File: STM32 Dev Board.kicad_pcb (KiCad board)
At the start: 2 copper layers, 41.1 x 50 mm, 33 parts, among them J5 2 Pin JST, J6 USB_B_Micro, Q1 PMOS, U1 FT230XS, U2 STM32F070F6Px, U3 MCP1824S, U4 MCP73113

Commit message: generated drill and gerber files, updeted a few datasheets
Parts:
- removed the D4 at (130.7, 97.0)
- removed the D4 at (127.8, 98.8)
- added C3: 7pF, Capacitor_SMD:C_0805_2012Metric_Pad1.18x1.45mm_HandSolder, F.Cu at (127.9, 85.0)
- added C4: 7pF, Capacitor_SMD:C_0805_2012Metric_Pad1.18x1.45mm_HandSolder, F.Cu at (127.9, 78.4)
- added D4: D_Schottky, Diode_SMD:D_SMF, B.Cu at (151.3, 85.1)
- added R9: 10k, Resistor_SMD:R_1206_3216Metric_Pad1.30x1.75mm_HandSolder, F.Cu at (124.3, 67.6)
- added X1: ~, MyLib:Xtal, F.Cu at (127.1, 82.8)
- J5: footprint Battery:BatteryHolder_MPD_BK-18650-PC2 -> Connector_PinHeader_2.00mm:PinHeader_1x02_P2.00mm_Vertical_SMD_Pin1Right
- SW2: moved to F.Cu
- U1: value FT230XS -> MCP2221AxML; footprint Package_SO:SSOP-16_3.9x4.9mm_P0.635mm -> Package_DFN_QFN:QFN-16-1EP_4x4mm_P0.65mm_EP2.5x2.5mm
- moved J5 86.5 mm to (155.3, 88.1), turned to 180 degrees
- moved J7 50.9 mm to (134.0, 67.7), turned to 0 degrees
- moved J6 46.5 mm to (141.3, 68.8), turned to 180 degrees
- moved SW2 40.8 mm to (125.3, 72.2), turned to -90 degrees
- moved R3 40.5 mm to (141.8, 73.6), turned to 180 degrees
- moved J3 37.1 mm to (130.4, 75.3), turned to 180 degrees
- moved R8 32.0 mm to (151.3, 80.1)
- moved D3 31.1 mm to (156.6, 84.2), turned to -90 degrees
- moved U1 29.9 mm to (140.2, 77.5)
- moved R7 27.7 mm to (153.6, 85.2), turned to -90 degrees
- moved R5 22.0 mm to (156.1, 72.3), turned to 0 degrees
- moved Q1 21.3 mm to (147.6, 81.3)
- moved R4 21.2 mm to (155.6, 75.9), turned to -90 degrees
- moved D1 20.9 mm to (152.8, 69.2), turned to 0 degrees
- moved U4 17.0 mm to (152.8, 72.6), turned to 180 degrees
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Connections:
- J7 pad 3: UART_Rx -> UART_Tx
- J7 pad 4: UART_Tx -> UART_Rx
- R3 pad 1: Net-(U1-~{RESET}) -> VUSB
- R3 pad 2: VUSB -> Net-(U1-~{RST})
- SW2 pad 1: GND -> Net-(R9-Pad1)
- U1 pad 1: UART_Tx -> unconnected-(U1-GP0-Pad1)
- U1 pad 10: Net-(U1-3V3OUT) -> VUSB
- U1 pad 11: Net-(U1-~{RESET}) -> Net-(J6-D-)
- U1 pad 12: VUSB -> Net-(J6-D+)
- U1 pad 16: unconnected-(U1-CBUS3-Pad16) -> VUSB
- U1 pad 3: Net-(U1-3V3OUT) -> Net-(U1-~{RST})
- U1 pad 4: UART_Rx -> UART_Tx
- U1 pad 5: GND -> UART_Rx
- U1 pad 8: Net-(J6-D+) -> unconnected-(U1-SDA-Pad8)
- U1 pad 9: Net-(J6-D-) -> unconnected-(U1-SCL-Pad9)
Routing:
- net Net-(SW2-C): track 0.00 -> 27.4 mm
- net /PSU/BAT+: track 29.9 -> 3.20 mm
- net Net-(U2-PB1): track 27.3 -> 10.4 mm
- net Net-(J6-D+): track 21.8 -> 6.24 mm
- net 3.3V: track 68.4 -> 53.5 mm, vias 4 -> 6
- net Net-(J6-D-): track 22.7 -> 7.69 mm
- net VUSB: track 43.5 -> 56.6 mm, vias 1 -> 2
- net /MCU/SWCLK: track 4.68 -> 15.7 mm
- net Net-(D2-K): track 19.4 -> 30.2 mm, vias 0 -> 1
- net GND: track 28.9 -> 20.0 mm, vias 42 -> 47
- net Net-(U1-~{RESET}): track 8.17 -> 0.00 mm
- net Net-(D4-A): track 0.00 -> 7.62 mm
- net Net-(U1-~{RST}): track 0.00 -> 7.44 mm
- net Net-(U2-PF1): track 8.20 -> 15.5 mm
- net /MCU/SWD: track 6.92 -> 14.0 mm
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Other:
- board size 41.1 x 50 mm -> 38.5 x 32.7 mm
- board text added: "5V 5V Tx Rx"
- board text added: "A10 A9 A7 A6 A5"
- board text added: "F0 F1 A0 A1 A4"
- board text added: "GND CLK SWD 3V3 RST"
- board text added: "GND GND 3V3 3V3"
- board text added: "Tyler Hickling STM32F070 Prototype Board V2.0 JUN/2026"
- board text removed: "3.3"
- board text removed: "GND"
- board text removed: "NRST 3.3 SWD SCLK GND"
- board text removed: "PA10 PA9 PA7 PA6 PA5"
- board text removed: "PF0 PF1 PA0 PA1 PA4"

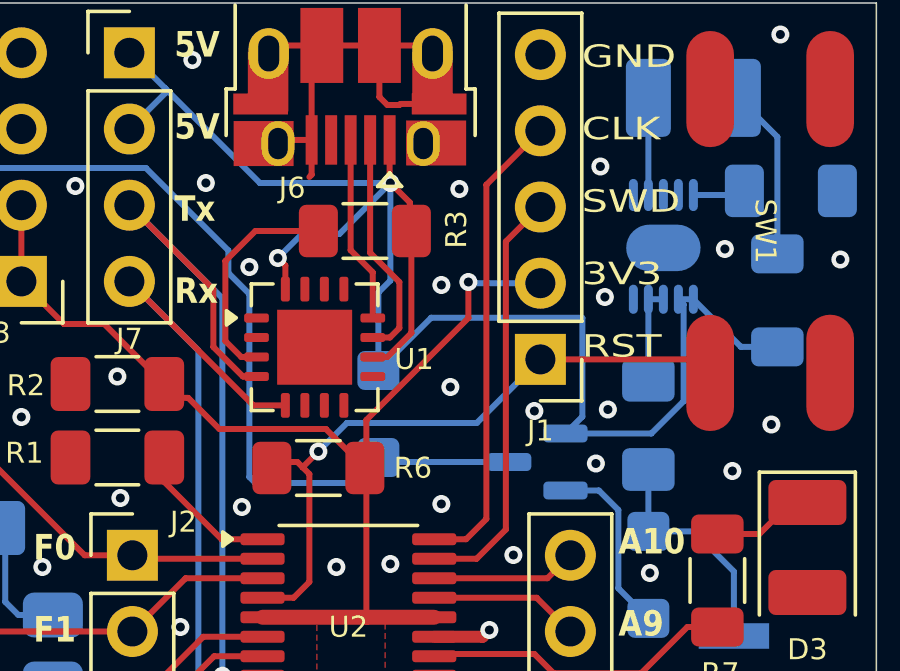
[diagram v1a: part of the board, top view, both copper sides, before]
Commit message: changed R8 FP to match component
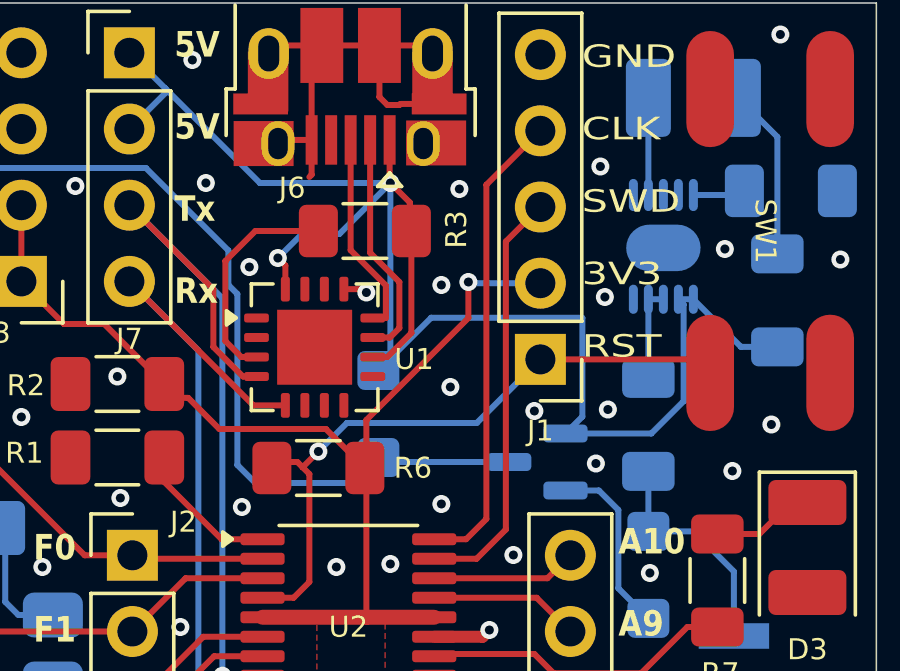
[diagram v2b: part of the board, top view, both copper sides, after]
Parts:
- D4: value D_Schottky -> V1FM10-M3/H
- R8: footprint LED_SMD:LED_1206_3216Metric_Pad1.42x1.75mm_HandSolder -> Resistor_SMD:R_1206_3216Metric_Pad1.30x1.75mm_HandSolder
- U1: value MCP2221AxML -> MCP2221A-I/ML
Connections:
- net 3.3V renamed +3.3V
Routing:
- net GND: track 20.0 -> 20.8 mm, vias 47 -> 48
- net Net-(J6-D+): track 6.24 -> 6.86 mm
